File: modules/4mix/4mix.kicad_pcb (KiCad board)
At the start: 4 copper layers, 91.4 x 68.6 mm, 168 parts, among them U1 MCP6002-xSN, U10 MCP6002-xSN, U11 MCP6002-xSN, U2 MCP6002-xSN, U3 MCP6002-xSN, U4 MCP6002-xSN, U5 MCP6002-xSN, U6 MCP6002-xSN, U7 MCP6002-xSN, U8 MCP6002-xSN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

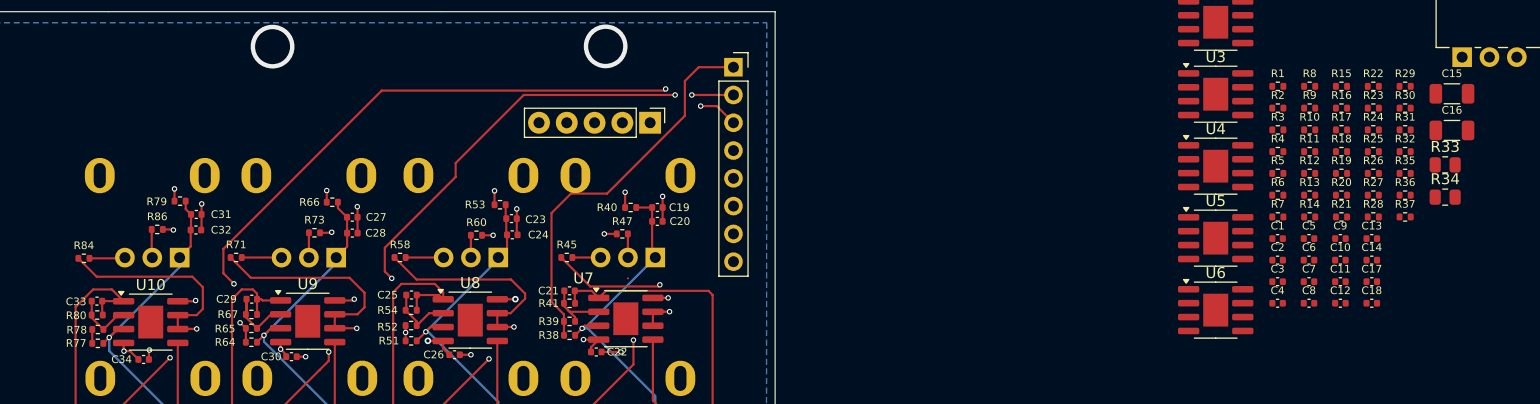
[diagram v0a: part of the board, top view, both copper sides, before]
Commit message: Add vmid routing
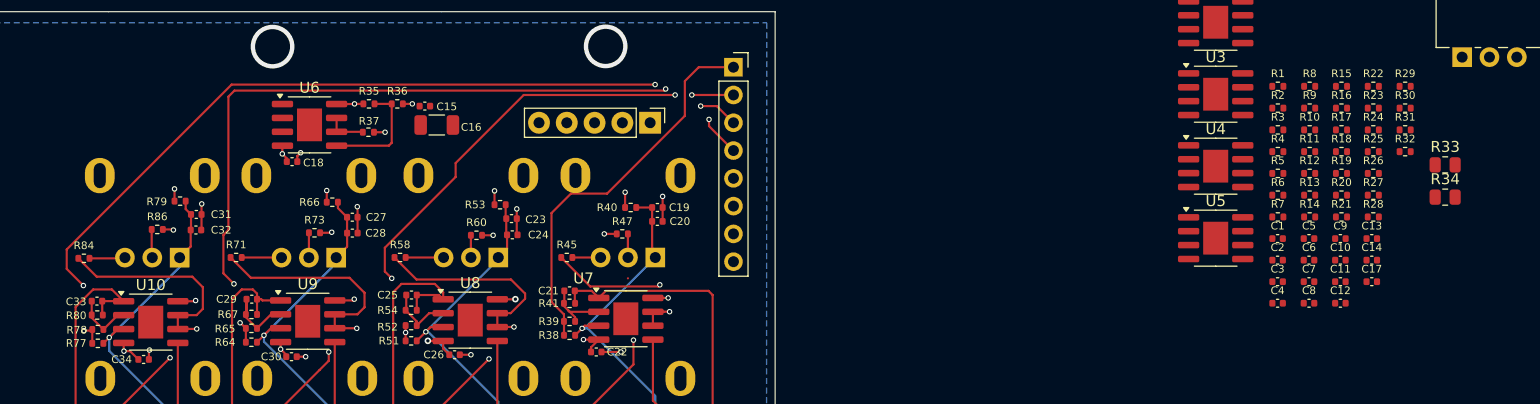
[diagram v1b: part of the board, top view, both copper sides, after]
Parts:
- C15: footprint Capacitor_SMD:C_1206_3216Metric -> Capacitor_SMD:C_0402_1005Metric
- moved C18 99.6 mm to (94.3, 54.4), turned to 180 degrees
- moved R37 95.1 mm to (101.2, 51.7)
- moved R35 94.9 mm to (101.3, 49.1)
- moved C15 93.9 mm to (106.4, 49.3)
- moved C16 92.8 mm to (107.5, 51.0)
- moved R36 92.5 mm to (103.9, 49.1)
- moved U6 84.6 mm to (95.9, 51.0)
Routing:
- net IN_4: track 1.27 -> 81.5 mm, vias 0 -> 4
- net Net-(U6B-+): track 0.00 -> 10.3 mm
- net IN_3: track 64.0 -> 71.9 mm
- net Net-(U6B--): track 0.00 -> 3.68 mm
- net V_SUPPLY: track 11.0 -> 14.4 mm, vias 8 -> 10
- net GND: track 19.2 -> 21.7 mm, vias 8 -> 10
- net V_MID: track 4.85 -> 5.87 mm, vias 5 -> 6

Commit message: Add routes for mian mix
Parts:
- removed R9: 100, Resistor_SMD:R_0402_1005Metric
- RV17, RV2, RV3: moved to B.Cu
- moved RV17 197.1 mm to (53.9, 74.7), turned to 180 degrees
- moved RV3 155.2 mm to (67.0, 74.7), turned to 180 degrees
- moved R44 153.2 mm to (71.8, 89.6), turned to 180 degrees
- moved R70 150.7 mm to (71.8, 87.4), turned to 180 degrees
- moved RV2 138.2 mm to (66.9, 56.1), turned to 180 degrees
- moved R10 134.8 mm to (61.5, 99.9)
- moved R1 129.5 mm to (61.4, 87.9), turned to 180 degrees
- moved R11 129.4 mm to (61.9, 85.3), turned to 180 degrees
- moved R2 128.5 mm to (61.4, 86.7)
- moved U1 123.3 mm to (67.0, 87.2)
- moved R8 121.2 mm to (71.7, 83.9), turned to 180 degrees
- moved C4 114.1 mm to (71.7, 85.2)
- moved R83 110.9 mm to (71.8, 88.5), turned to 180 degrees
- moved R57 107.1 mm to (71.8, 86.4), turned to 180 degrees
- moved R82 5.68 mm to (81.0, 97.4), turned to 180 degrees
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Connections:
- C15 pad 2: Net-(U6B-+) -> GND
- C16 pad 2: Net-(U6B-+) -> GND
- R11 pad 1: Net-(R11-Pad1) -> Net-(C3-Pad1)
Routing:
- net V_MID: track 5.87 -> 179.0 mm, vias 6 -> 7
- net IN_MIXOUT: track 0.00 -> 123.1 mm
- net Net-(R43-Pad2): track 0.89 -> 64.6 mm, vias 1 -> 2
- net Net-(R56-Pad2): track 1.14 -> 44.1 mm, vias 1 -> 2
- net Net-(C4-Pad1): track 0.00 -> 36.5 mm, vias 0 -> 2
- net Net-(R69-Pad2): track 0.89 -> 29.1 mm, vias 1 -> 2
- net MAIN_MIX: track 0.00 -> 20.9 mm, vias 0 -> 2
- net Net-(R82-Pad2): track 1.12 -> 15.2 mm, vias 1 -> 2
- net V_SUPPLY: track 14.4 -> 19.4 mm, vias 10 -> 12
- net GND: track 21.7 -> 26.3 mm, vias 10 -> 12
- net Net-(U6B-+): track 10.3 -> 14.7 mm
- net Net-(U9B-+): track 35.7 -> 32.6 mm
- net Net-(U10B-+): track 35.5 -> 32.6 mm
- net Net-(U8B-+): track 34.9 -> 32.2 mm
- net Net-(R10-Pad2): track 0.00 -> 2.67 mm
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
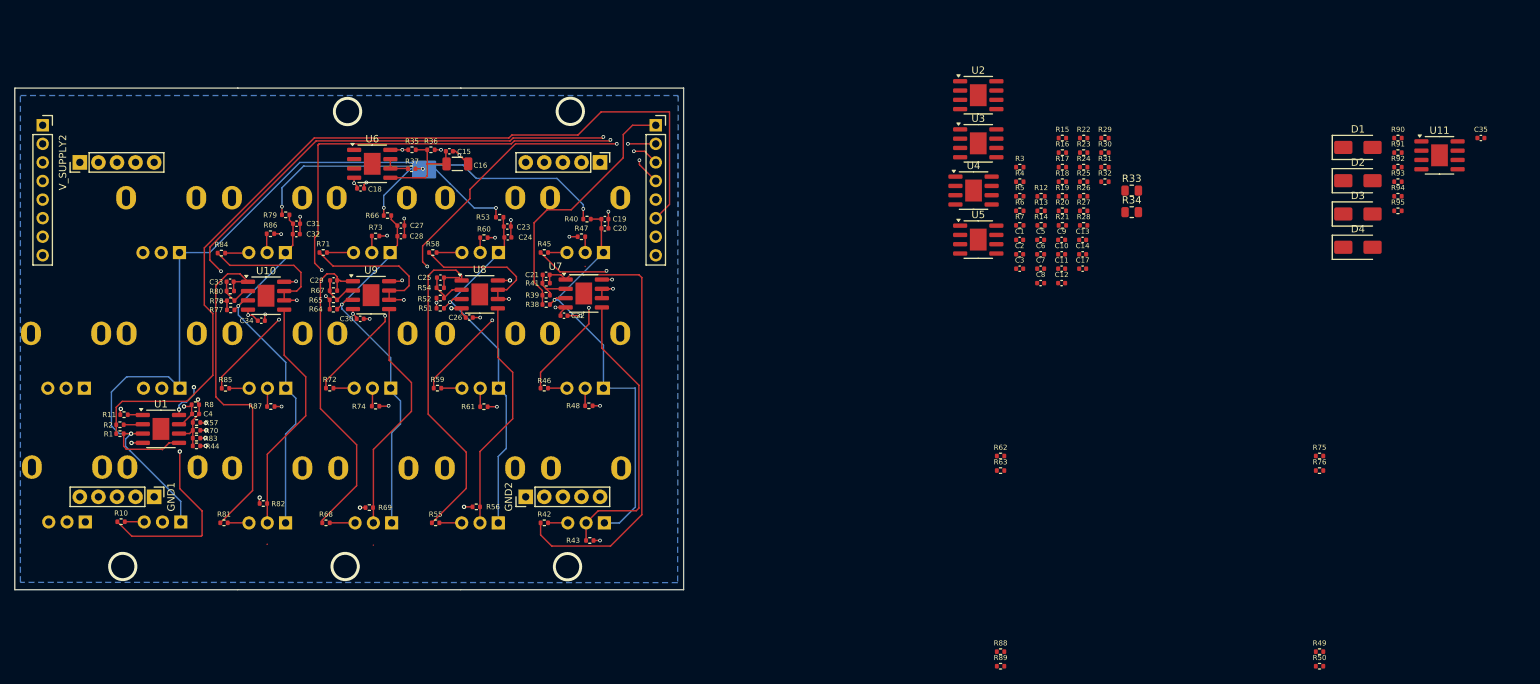
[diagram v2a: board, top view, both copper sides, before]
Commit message: Add sends routing
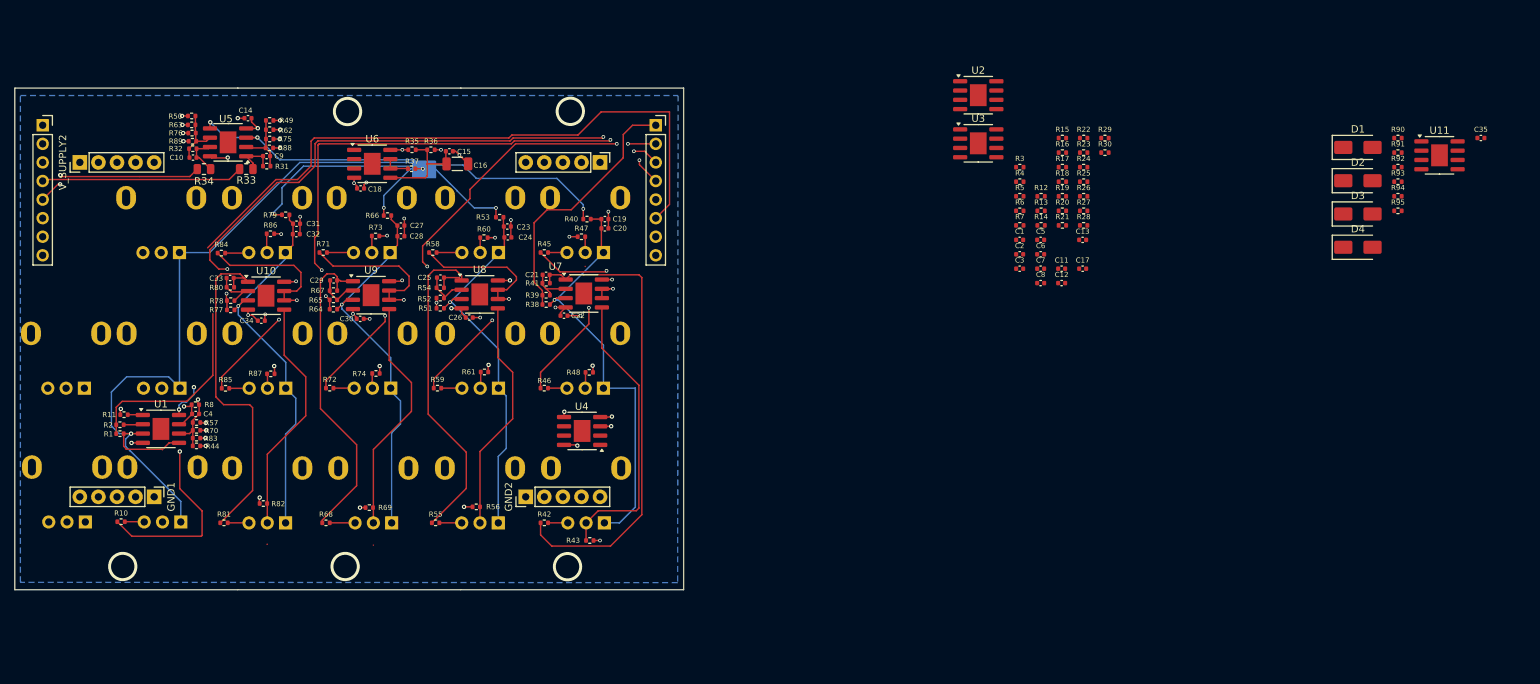
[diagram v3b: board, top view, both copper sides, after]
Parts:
- moved R50 171.6 mm to (71.2, 44.5)
- moved R76 160.9 mm to (71.2, 46.8)
- moved R49 160.9 mm to (81.8, 45.1), turned to 180 degrees
- moved R75 149.9 mm to (81.8, 47.6), turned to 180 degrees
- moved R89 131.8 mm to (71.3, 47.9)
- moved R34 127.0 mm to (72.8, 51.7), turned to 180 degrees
- moved R32 124.8 mm to (71.3, 48.9)
- moved R88 121.4 mm to (81.8, 48.8), turned to 180 degrees
- moved R33 121.1 mm to (78.6, 51.7), turned to 180 degrees
- moved R63 120.3 mm to (71.2, 45.7)
- moved C10 119.5 mm to (71.4, 50.1), turned to 180 degrees
- moved C14 115.6 mm to (78.9, 44.8)
- moved R31 114.6 mm to (81.4, 51.3), turned to 180 degrees
- moved R62 109.4 mm to (81.8, 46.3), turned to 180 degrees
- moved C9 109.3 mm to (81.4, 49.9)
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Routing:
- net Net-(R48-Pad2): track 1.02 -> 88.6 mm, vias 1 -> 2
- net Net-(R61-Pad2): track 1.27 -> 73.8 mm, vias 1 -> 2
- net Net-(R74-Pad2): track 1.29 -> 58.3 mm, vias 1 -> 2
- net Net-(R47-Pad2): track 1.14 -> 56.3 mm, vias 1 -> 2
- net Net-(R60-Pad2): track 1.02 -> 45.2 mm, vias 1 -> 2
- net Net-(R87-Pad2): track 0.97 -> 43.3 mm, vias 1 -> 2
- net V_MID: track 179.0 -> 217.1 mm, vias 7 -> 11
- net Net-(R73-Pad2): track 1.09 -> 29.4 mm, vias 1 -> 2
- net SEND_A_OUT: track 0.00 -> 27.6 mm
- net SEND_B_OUT: track 0.00 -> 23.8 mm, vias 0 -> 2
- net Net-(R86-Pad2): track 0.99 -> 14.0 mm, vias 1 -> 2
- net SEND_A_MIX: track 0.00 -> 9.25 mm
- net SEND_B_MIX: track 0.00 -> 8.25 mm
- net IN_MIXOUT: track 123.1 -> 115.2 mm
- net Net-(C9-Pad1): track 0.00 -> 5.83 mm
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
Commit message: Complete sends routing
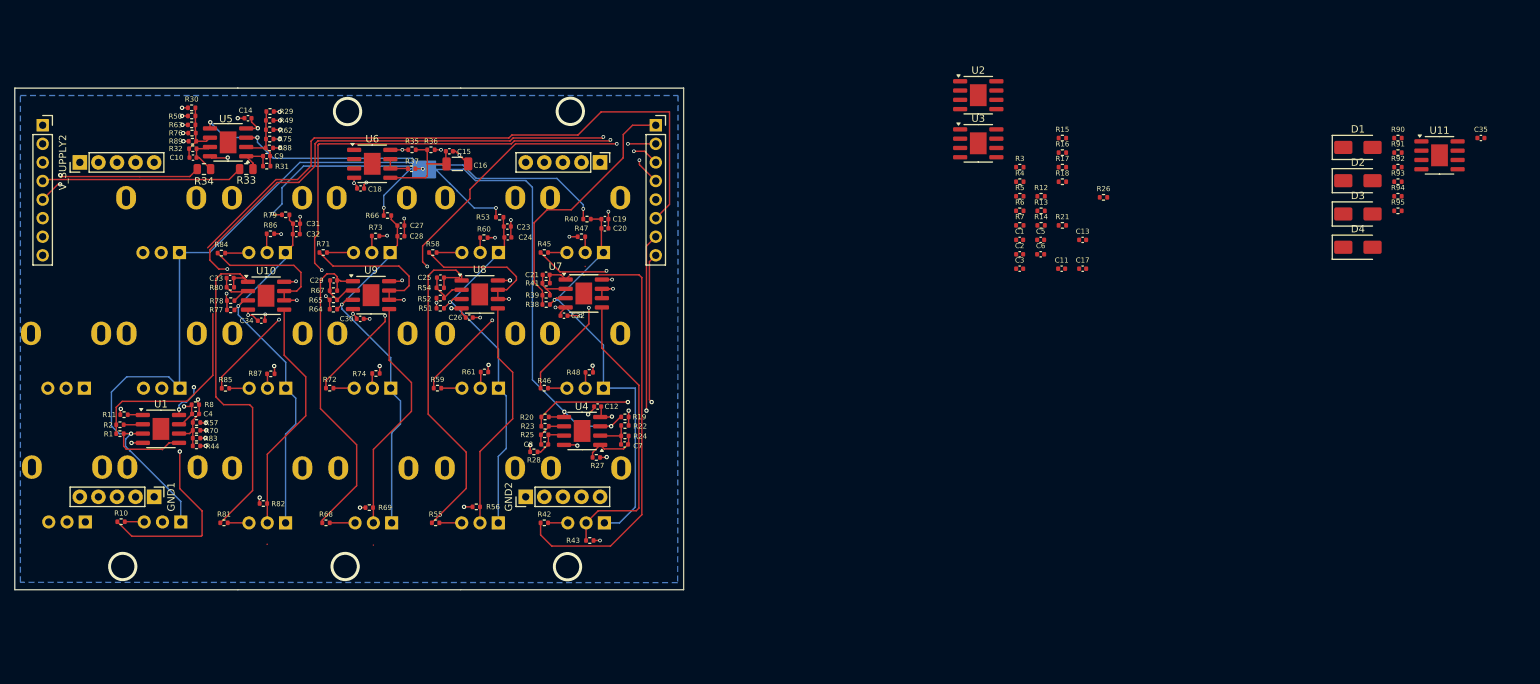
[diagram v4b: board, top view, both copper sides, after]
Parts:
- moved R30 125.0 mm to (71.2, 43.3)
- moved R29 114.2 mm to (81.9, 43.8), turned to 180 degrees
- moved R23 82.6 mm to (119.5, 86.9)
- moved R25 81.4 mm to (119.4, 88.0)
- moved R28 81.3 mm to (118.0, 90.4), turned to 180 degrees
- moved R20 76.1 mm to (119.5, 85.6), turned to 180 degrees
- moved R27 74.7 mm to (126.5, 91.1)
- moved R22 74.0 mm to (130.4, 86.8), turned to 180 degrees
- moved R24 72.7 mm to (130.4, 88.2)
- moved C8 71.3 mm to (119.4, 89.4), turned to 180 degrees
- moved R19 67.0 mm to (130.4, 85.6)
- moved C12 65.6 mm to (126.7, 84.2)
- moved C7 61.8 mm to (130.3, 89.4), turned to 180 degrees
- moved R26 2.72 mm to (195.8, 55.6)
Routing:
- net Net-(R28-Pad2): track 0.00 -> 106.1 mm, vias 0 -> 2
- net Net-(R27-Pad2): track 0.00 -> 87.6 mm, vias 0 -> 2
- net V_MID: track 217.1 -> 277.1 mm
- net IN_SEND_B: track 0.00 -> 37.8 mm, vias 0 -> 2
- net IN_SEND_A: track 0.00 -> 28.8 mm, vias 0 -> 2
- net Net-(C7-Pad1): track 0.00 -> 7.63 mm
- net Net-(U4A--): track 0.00 -> 5.50 mm
- net Net-(C8-Pad1): track 0.00 -> 5.39 mm
- net Net-(U4B--): track 0.00 -> 4.97 mm
- net GND: track 31.3 -> 32.8 mm
- net V_SUPPLY: track 24.7 -> 26.1 mm, vias 15 -> 16
- net SEND_A_MIX: track 9.25 -> 10.5 mm
- net SEND_B_MIX: track 8.25 -> 9.37 mm

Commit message: Add return buffering
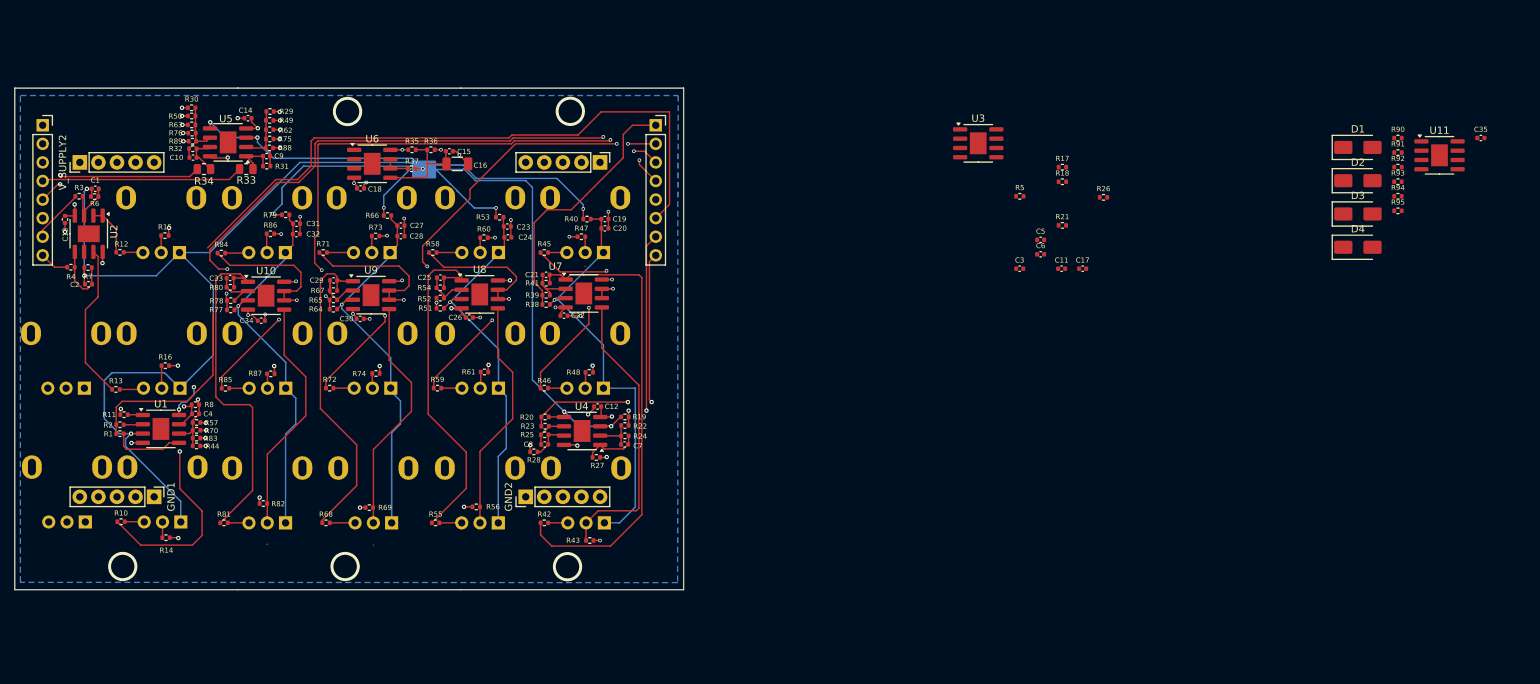
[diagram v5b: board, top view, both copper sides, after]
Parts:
- moved C13 139.2 mm to (53.8, 58.6), turned to 90 degrees
- moved R4 130.3 mm to (54.7, 65.1)
- moved R13 128.8 mm to (60.8, 81.8)
- moved R3 128.7 mm to (55.8, 55.4)
- moved R7 127.5 mm to (57.0, 65.2)
- moved C2 127.4 mm to (57.1, 67.5)
- moved R14 127.0 mm to (67.7, 102.1)
- moved C1 126.6 mm to (58.0, 54.4)
- moved R6 126.5 mm to (57.9, 55.5)
- moved R12 126.2 mm to (61.4, 63.1)
- moved R16 126.1 mm to (67.6, 78.6)
- moved R15 123.4 mm to (67.5, 60.8)
- moved U2 123.1 mm to (57.1, 60.6), turned to -90 degrees
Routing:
- net V_MID: track 277.1 -> 314.1 mm, vias 11 -> 13
- net Net-(U2B--): track 0.00 -> 21.3 mm
- net Net-(U2B-+): track 0.00 -> 9.35 mm
- net RETURN_A: track 0.00 -> 7.39 mm
- net Net-(U2A-+): track 0.00 -> 7.23 mm
- net Net-(U2A--): track 0.00 -> 7.05 mm
- net RETURN_B: track 0.00 -> 4.03 mm
- net Net-(U3A--): track 0.00 -> 3.49 mm, vias 0 -> 3
- net Net-(R13-Pad2): track 0.00 -> 3.33 mm
- net Net-(R16-Pad1): track 0.00 -> 3.09 mm
- net GND: track 32.8 -> 35.7 mm, vias 14 -> 15
- net V_SUPPLY: track 26.1 -> 28.9 mm, vias 16 -> 18
- net Net-(R12-Pad2): track 0.00 -> 2.65 mm
- net Net-(R15-Pad1): track 0.00 -> 2.32 mm
- net Net-(R14-Pad1): track 0.00 -> 2.16 mm
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
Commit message: Finalized main routing of the board
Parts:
- moved R17 129.8 mm to (61.4, 67.7)
- moved R5 128.4 mm to (59.5, 85.2)
- moved C17 127.8 mm to (65.5, 73.3), turned to 180 degrees
- moved C11 127.2 mm to (65.5, 90.8), turned to 180 degrees
- moved C3 127.0 mm to (59.4, 87.8), turned to 180 degrees
- moved R18 126.0 mm to (64.8, 66.2)
- moved C5 126.0 mm to (61.4, 69.1), turned to 180 degrees
- moved R26 124.1 mm to (72.2, 66.9)
- moved R21 118.4 mm to (72.3, 70.3), turned to 180 degrees
- moved C6 115.1 mm to (72.3, 69.0)
- moved U3 113.9 mm to (66.9, 69.6)
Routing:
- net Net-(U3A--): track 3.49 -> 106.1 mm, vias 3 -> 4
- net MIXOUT: track 0.00 -> 39.2 mm, vias 0 -> 1
- net V_MID: track 314.1 -> 331.6 mm, vias 13 -> 16
- net Net-(U3B--): track 0.00 -> 14.3 mm, vias 0 -> 2
- net Net-(U1A--): track 2.64 -> 11.2 mm, vias 0 -> 2
- net Net-(C3-Pad1): track 2.07 -> 10.0 mm, vias 0 -> 2
- net /Overdrive/INPUT: track 0.00 -> 5.97 mm
- net Net-(C5-Pad1): track 0.00 -> 5.38 mm
- net GND: track 35.7 -> 41.0 mm, vias 15 -> 16
- net V_SUPPLY: track 28.9 -> 32.4 mm, vias 18 -> 21
